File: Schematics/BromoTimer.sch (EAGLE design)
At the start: 29 parts, among them IC1 PIC16F687, IC2 7805TV, K1 G2R2A, K2 G2R2A, Q1 BC548B, Q2 BC548B, Q3 BC548B, X1 AC_IN, X4 22-23-2041, X5 AC_OUT

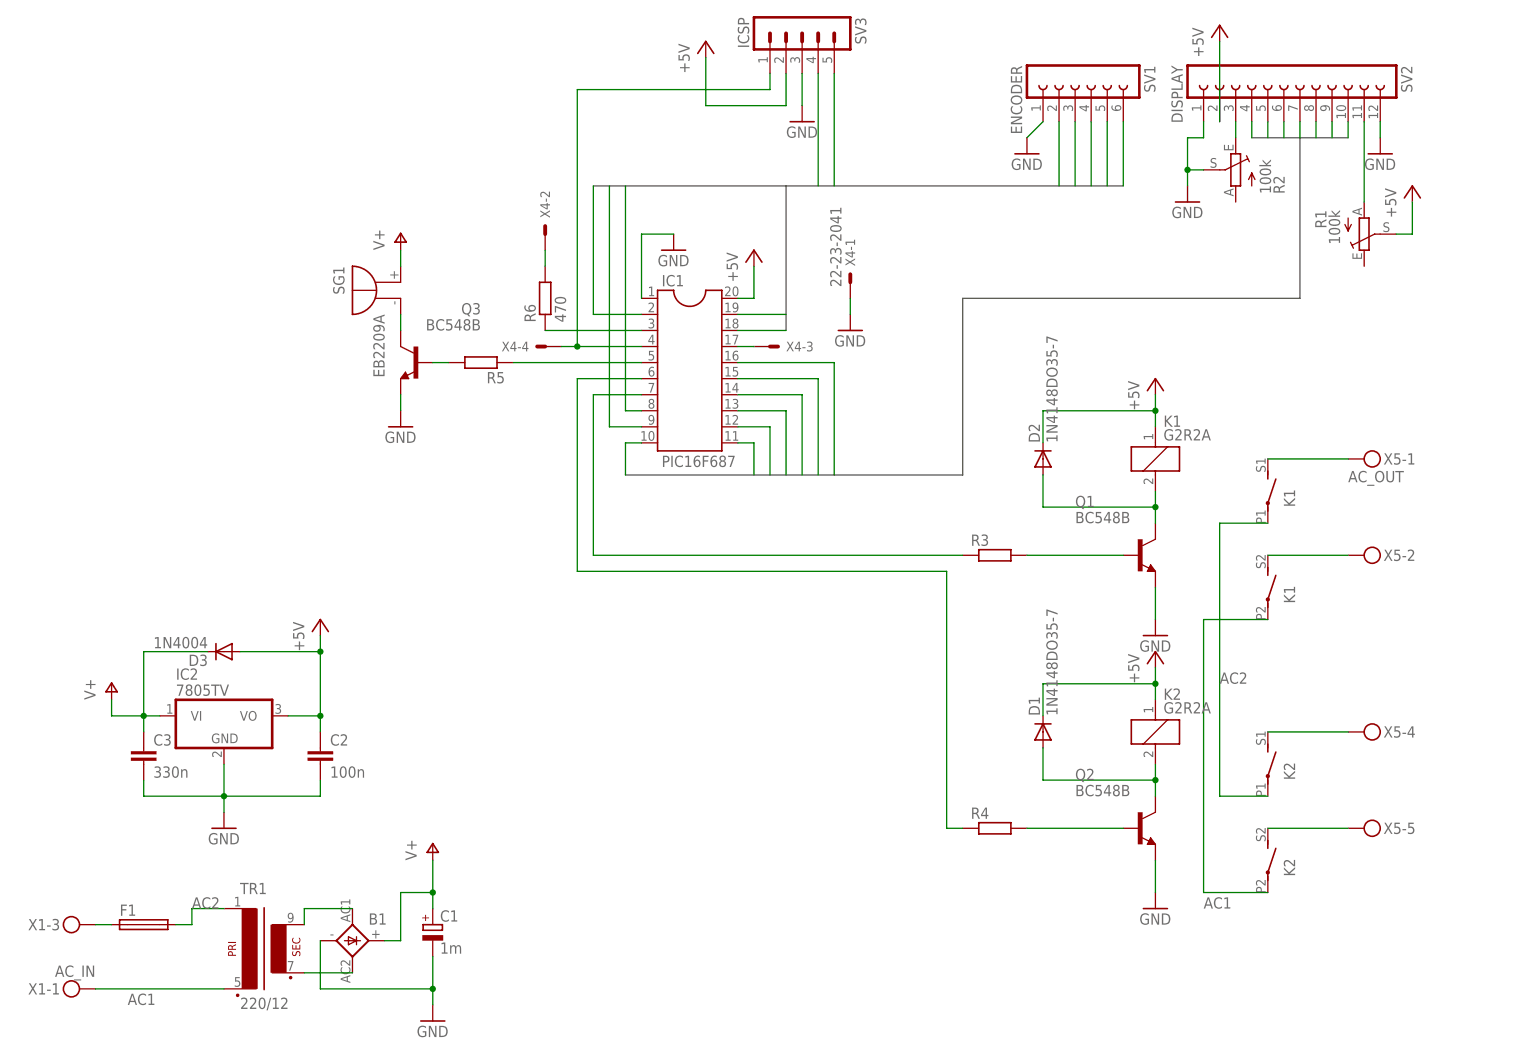
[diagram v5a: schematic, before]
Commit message: New PCB prototype
The new PCB is a little taller and a lot less wide. It has extra space for the
7805 heatsink. Connector layout should be better, too.
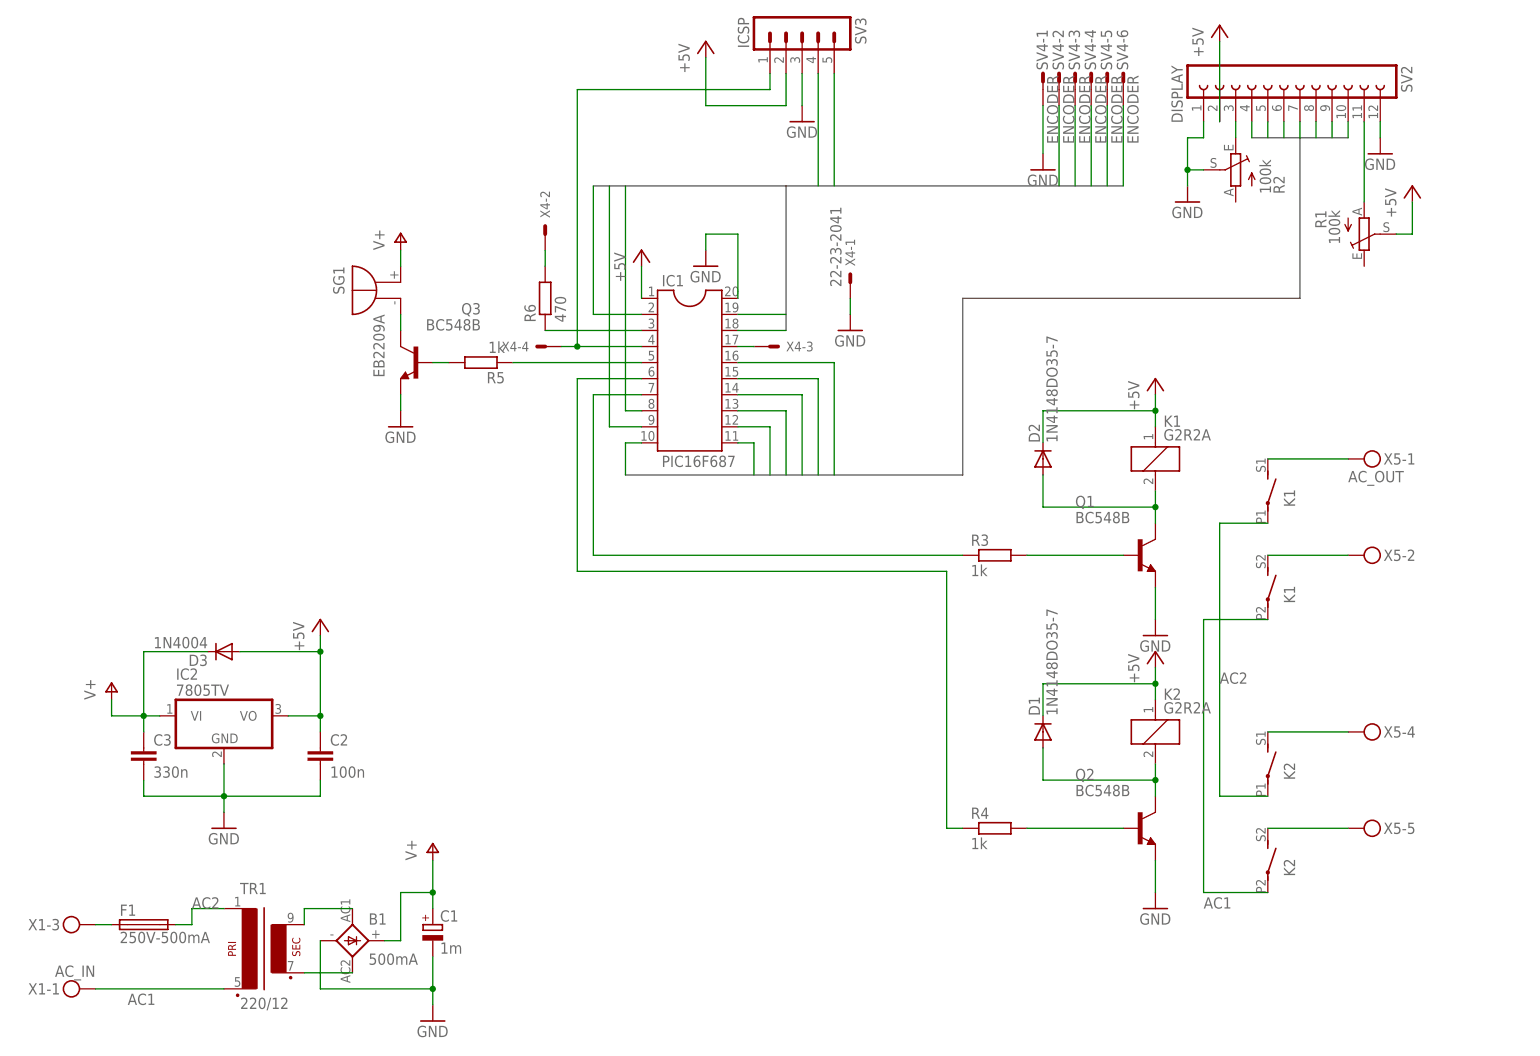
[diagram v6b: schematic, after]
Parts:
- removed SV1: ENCODER, con-lsta:FE06-1
- added SV4: ENCODER, con-amp-mt:L06P
- B1: value (none) -> 500mA
- F1: value (none) -> 250V-500mA
- R1, R2: device pot:TRIM_EU-CA14H -> pot:TRIM_EU-CA6V
- R3, R4, R5: value (none) -> 1k
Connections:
- net +5V: now also IC1.1; no longer IC1.20
- net A: now also SV4-5.S; no longer SV1.5
- net B: now also SV4-6.S; no longer SV1.6
- net GND: now also IC1.20, SV4-1.S; no longer IC1.1, SV1.1
- net L1: now also SV4-2.S; no longer SV1.2
- net L2: now also SV4-3.S; no longer SV1.3
- net SW: now also SV4-4.S; no longer SV1.4
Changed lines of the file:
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@@
 </variantdefs>
 <classes>
-<class number="0" name="default" width="0.4064" drill="0">
-<clearance class="0" value="0.635"/>
+<class number="0" name="default" width="0.3048" drill="0">
+<clearance class="0" value="0.254"/>
 </class>
 <class number="1" name="HV" width="1.27" drill="0">
-<clearance class="1" value="1.27"/>
+<clearance class="1" value="0.635"/>
 </class>
 </classes>
@@
 <part name="IC1" library="ic-package" deviceset="DIL20" device="S" value="PIC16F687"/>
 <part name="FRAME1" library="frames" deviceset="A4L-LOC" device="" value="Draft2"/>
-<part name="SV1" library="con-lsta" deviceset="FE06-1" device="" value="ENCODER"/>
 <part name="SV2" library="con-lsta" deviceset="FE12-1" device="" value="DISPLAY"/>
 <part name="IC2" library="linear" deviceset="78*" device="TV" technology="05"/>
@@
 <part name="GND4" library="supply1" deviceset="GND" device=""/>
 <part name="P+3" library="supply1" deviceset="+5V" device=""/>
-<part name="R1" library="pot" deviceset="TRIM_EU-" device="CA14H" value="100k"/>
-<part name="R2" library="pot" deviceset="TRIM_EU-" device="CA14H" value="100k"/>
+<part name="R1" library="pot" deviceset="TRIM_EU-" device="CA6V" value="100k"/>
+<part name="R2" library="pot" deviceset="TRIM_EU-" device="CA6V" value="100k"/>
 <part name="P+4" library="supply1" deviceset="+5V" device=""/>
 <part name="Q1" library="transistor-npn" deviceset="BC548*" device="" technology="B" value="BC548B"/>
 <part name="Q2" library="transistor-npn" deviceset="BC548*" device="" technology="B" value="BC548B"/>
-<part name="R3" library="rcl" deviceset="R-EU_" device="0207/10"/>
-<part name="R4" library="rcl" deviceset="R-EU_" device="0207/10"/>
+<part name="R3" library="rcl" deviceset="R-EU_" device="0207/10" value="1k"/>
+<part name="R4" library="rcl" deviceset="R-EU_" device="0207/10" value="1k"/>
 <part name="GND5" library="supply1" deviceset="GND" device=""/>
 <part name="GND6" library="supply1" deviceset="GND" device=""/>
@@
 <attribute name="OC_NEWARK" value="36M5257"/>
 </part>
-<part name="B1" library="rectifier" deviceset="2KBB-R" device=""/>
+<part name="B1" library="rectifier" deviceset="2KBB-R" device="" value="500mA"/>
 <part name="P+7" library="supply1" deviceset="V+" device=""/>
 <part name="GND7" library="supply1" deviceset="GND" device=""/>
@@
 <part name="D3" library="diode" deviceset="1N4004" device=""/>
 <part name="Q3" library="transistor-npn" deviceset="BC548*" device="" technology="B" value="BC548B"/>
-<part name="R5" library="rcl" deviceset="R-EU_" device="0207/10"/>
+<part name="R5" library="rcl" deviceset="R-EU_" device="0207/10" value="1k"/>
 <part name="GND11" library="supply1" deviceset="GND" device=""/>
 <part name="P+10" library="supply1" deviceset="V+" device=""/>
@@
 <part name="X1" library="con-phoenix-508" deviceset="MKDSN1,5/3-5,08" device="" value="AC_IN"/>
 <part name="X5" library="con-phoenix-508" deviceset="MKDSN1,5/5-5,08" device="" value="AC_OUT"/>
-<part name="F1" library="fuse" deviceset="SH22" device="">
+<part name="F1" library="fuse" deviceset="SH22" device="" value="250V-500mA">
 <attribute name="MPN" value=""/>
 <attribute name="OC_FARNELL" value="unknown"/>
 <attribute name="OC_NEWARK" value="unknown"/>
 </part>
+<part name="SV4" library="con-amp-mt" deviceset="L06P" device="" value="ENCODER"/>
 </parts>
 <sheets>
@@
 <instance part="IC1" gate="G$1" x="114.3" y="116.84"/>
 <instance part="FRAME1" gate="G$1" x="0" y="0"/>
-<instance part="SV1" gate="G$1" x="175.26" y="162.56" rot="R270"/>
 <instance part="SV2" gate="G$1" x="208.28" y="162.56" rot="R270"/>
 <instance part="IC2" gate="A1" x="40.64" y="60.96"/>
@@
 <instance part="C1" gate="G$1" x="73.66" y="27.94"/>
 <instance part="C2" gate="G$1" x="55.88" y="55.88"/>
-<instance part="GND2" gate="1" x="111.76" y="134.62"/>
-<instance part="P+2" gate="1" x="124.46" y="134.62"/>
+<instance part="GND2" gate="1" x="116.84" y="132.08"/>
+<instance part="P+2" gate="1" x="106.68" y="134.62"/>
 <instance part="GND3" gate="1" x="193.04" y="142.24"/>
 <instance part="GND4" gate="1" x="223.52" y="149.86"/>
@@
 <instance part="GND7" gate="1" x="73.66" y="12.7"/>
 <instance part="P+8" gate="1" x="22.86" y="66.04"/>
-<instance part="GND8" gate="1" x="167.64" y="149.86"/>
+<instance part="GND8" gate="1" x="170.18" y="147.32"/>
 <instance part="P+5" gate="1" x="187.96" y="71.12"/>
 <instance part="P+6" gate="1" x="187.96" y="114.3"/>
@@
 <instance part="F1" gate="1" x="27.94" y="27.94"/>
 <instance part="X4" gate="-4" x="91.44" y="119.38" rot="R180"/>
+<instance part="SV4" gate="-1" x="170.18" y="162.56" rot="MR270"/>
+<instance part="SV4" gate="-2" x="172.72" y="162.56" rot="MR270"/>
+<instance part="SV4" gate="-3" x="175.26" y="162.56" rot="MR270"/>
+<instance part="SV4" gate="-4" x="177.8" y="162.56" rot="MR270"/>
+<instance part="SV4" gate="-5" x="180.34" y="162.56" rot="MR270"/>
+<instance part="SV4" gate="-6" x="182.88" y="162.56" rot="MR270"/>
 </instances>
 <busses>
@@
 <nets>
 <net name="+5V" class="0">
-<segment>
-<pinref part="P+2" gate="1" pin="+5V"/>
-<wire x1="124.46" y1="132.08" x2="124.46" y2="127" width="0.1524" layer="91"/>
-<pinref part="IC1" gate="G$1" pin="20"/>
-<wire x1="124.46" y1="127" x2="121.92" y2="127" width="0.1524" layer="91"/>
-</segment>
 <segment>
 <pinref part="SV2" gate="G$1" pin="2"/>
@@
 <wire x1="228.6" y1="137.16" x2="226.06" y2="137.16" width="0.1524" layer="91"/>
 </segment>
+<segment>
+<pinref part="IC1" gate="G$1" pin="1"/>
+<pinref part="P+2" gate="1" pin="+5V"/>
+<wire x1="106.68" y1="127" x2="106.68" y2="132.08" width="0.1524" layer="91"/>
+</segment>
 </net>
 <net name="GND" class="0">
@@
 </segment>
 <segment>
-<pinref part="IC1" gate="G$1" pin="1"/>
-<pinref part="GND2" gate="1" pin="GND"/>
-<wire x1="106.68" y1="127" x2="106.68" y2="137.16" width="0.1524" layer="91"/>
-<wire x1="106.68" y1="137.16" x2="111.76" y2="137.16" width="0.1524" layer="91"/>
-</segment>
-<segment>
 <pinref part="SV2" gate="G$1" pin="1"/>
 <pinref part="GND3" gate="1" pin="GND"/>
@@
 </segment>
 <segment>
-<pinref part="SV1" gate="G$1" pin="1"/>
-<pinref part="GND8" gate="1" pin="GND"/>
-<wire x1="170.18" y1="154.94" x2="167.64" y2="152.4" width="0.1524" layer="91"/>
-</segment>
-<segment>
 <pinref part="SV3" gate="G$1" pin="3"/>
 <pinref part="GND10" gate="1" pin="GND"/>
@@
 <wire x1="139.7" y1="124.46" x2="139.7" y2="127" width="0.1524" layer="91"/>
 </segment>
+<segment>
+<pinref part="IC1" gate="G$1" pin="20"/>
+<wire x1="121.92" y1="127" x2="121.92" y2="137.16" width="0.1524" layer="91"/>
+<pinref part="GND2" gate="1" pin="GND"/>
+<wire x1="121.92" y1="137.16" x2="116.84" y2="137.16" width="0.1524" layer="91"/>
+<wire x1="116.84" y1="137.16" x2="116.84" y2="134.62" width="0.1524" layer="91"/>
+</segment>
+<segment>
+<pinref part="GND8" gate="1" pin="GND"/>
+<pinref part="SV4" gate="-1" pin="S"/>
+<wire x1="170.18" y1="157.48" x2="170.18" y2="149.86" width="0.1524" layer="91"/>
+</segment>
 </net>
 <net name="RS" class="0">
@@
 <net name="L1" class="0">
 <segment>
-<pinref part="SV1" gate="G$1" pin="2"/>
-<wire x1="172.72" y1="154.94" x2="172.72" y2="144.78" width="0.1524" layer="91"/>
+<wire x1="172.72" y1="157.48" x2="172.72" y2="144.78" width="0.1524" layer="91"/>
+<pinref part="SV4" gate="-2" pin="S"/>
 </segment>
 <segment>
@@
 <net name="L2" class="0">
 <segment>
-<pinref part="SV1" gate="G$1" pin="3"/>
-<wire x1="175.26" y1="154.94" x2="175.26" y2="144.78" width="0.1524" layer="91"/>
+<wire x1="175.26" y1="157.48" x2="175.26" y2="144.78" width="0.1524" layer="91"/>
+<pinref part="SV4" gate="-3" pin="S"/>
 </segment>
 <segment>
@@
 <net name="SW" class="0">
 <segment>
-<pinref part="SV1" gate="G$1" pin="4"/>
-<wire x1="177.8" y1="154.94" x2="177.8" y2="144.78" width="0.1524" layer="91"/>
+<wire x1="177.8" y1="157.48" x2="177.8" y2="144.78" width="0.1524" layer="91"/>
+<pinref part="SV4" gate="-4" pin="S"/>
 </segment>
 <segment>
@@
 <net name="A" class="0">
 <segment>
-<pinref part="SV1" gate="G$1" pin="5"/>
-<wire x1="180.34" y1="154.94" x2="180.34" y2="144.78" width="0.1524" layer="91"/>
+<wire x1="180.34" y1="157.48" x2="180.34" y2="144.78" width="0.1524" layer="91"/>
+<pinref part="SV4" gate="-5" pin="S"/>
 </segment>
 <segment>
@@
 <net name="B" class="0">
 <segment>
-<pinref part="SV1" gate="G$1" pin="6"/>
-<wire x1="182.88" y1="154.94" x2="182.88" y2="144.78" width="0.1524" layer="91"/>
+<pinref part="SV4" gate="-6" pin="S"/>
+<wire x1="182.88" y1="144.78" x2="182.88" y2="157.48" width="0.1524" layer="91"/>
 </segment>
 <segment>
@@
 </segment>
 </net>
-<net name="N$22" class="0">
+<net name="N$22" class="1">
 <segment>
 <pinref part="X1" gate="-3" pin="KL"/>

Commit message: Custom PIC part, minor layout changes
Schematic:
- changed encoder connector to right angle type
- rewired trimmer for LCD contrast, it needs to vary voltage, not resistance
- add net class for power line, specifying 24thou width and 12thou keepout
- LCD trimmers are 10k, not 100k
- add decoupling cap to IC1
- rename bus lines to LR and LG instead of L1 and L2
Board:
- moved power components on a slightly better place
- aligned diodes and resistors
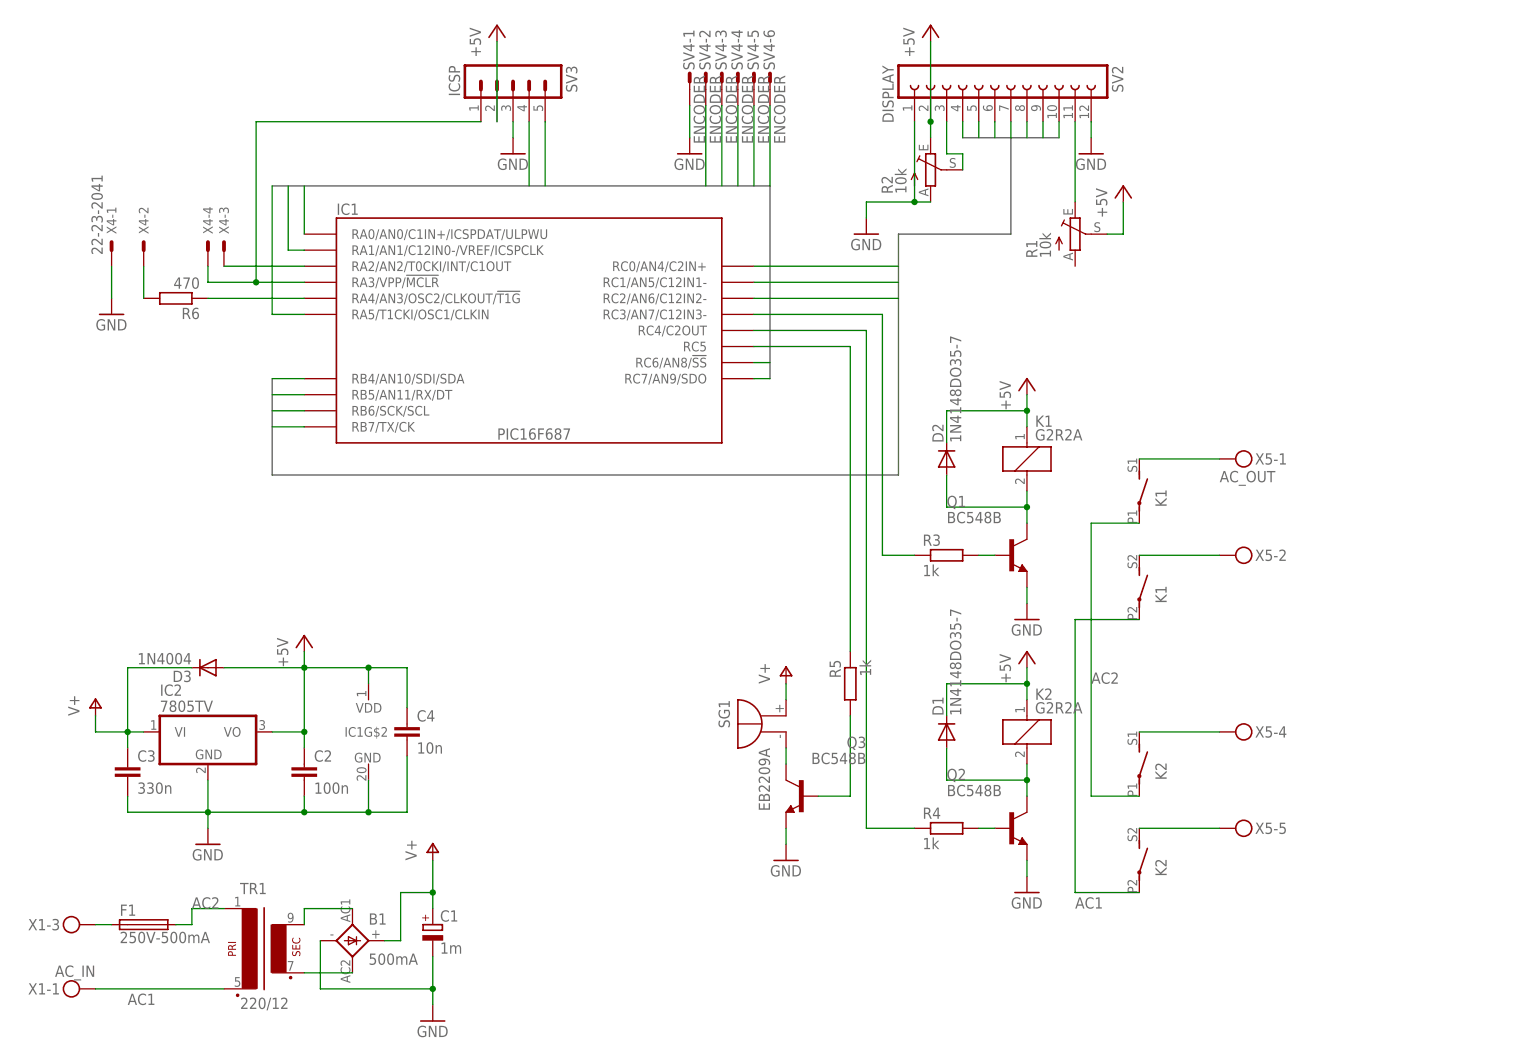
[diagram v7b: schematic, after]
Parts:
- added C4: 10n, rcl:C-EU025-024X044
- IC1: device ic-package:DIL20S -> g5pwlib:PIC16F687
- R1, R2: value 100k -> 10k
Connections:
- removed net L1: IC1.9, SV4-2.S
- removed net L2: IC1.8, SV4-3.S
- new net LG: IC1G$1.RC7/AN9/SDO, SV4-2.S
- new net LR: IC1G$1.RC6/AN8/!SS, SV4-3.S
- net +5V: now also C4.1, IC1G$2.VDD, R2.E; no longer IC1.1
- net A: now also IC1G$1.RA0/AN0/C1IN+/ICSPDAT/ULPWU; no longer IC1.19
- net B: now also IC1G$1.RA1/AN1/C12IN0-/VREF/ICSPCLK; no longer IC1.18
- net B0: now also IC1G$1.RB4/AN10/SDI/SDA; no longer IC1.13
- net B1: now also IC1G$1.RB5/AN11/RX/DT; no longer IC1.12
- net B2: now also IC1G$1.RB6/SCK/SCL; no longer IC1.11
- net B3: now also IC1G$1.RB7/TX/CK; no longer IC1.10
- net EN: now also IC1G$1.RC0/AN4/C2IN+; no longer IC1.16
- net GND: now also C4.2, IC1G$2.GND, R2.A; no longer IC1.20, R2.S
- net N$1: now also R1.E; no longer R1.A
- net N$13: now also IC1G$1.RA2/AN2/T0CKI/INT/C1OUT; no longer IC1.17
- net N$14: now also IC1G$1.RC4/C2OUT; no longer IC1.6
- net N$15: now also IC1G$1.RA3/VPP/!MCLR; no longer IC1.4
- net N$16: now also IC1G$1.RC3/AN7/C12IN3-; no longer IC1.7
- net N$17: now also IC1G$1.RC5; no longer IC1.5
- net N$20: now also IC1G$1.RA4/AN3/OSC2/CLKOUT/!T1G; no longer IC1.3
- net N$3: now also R2.S; no longer R2.E
- net RS: now also IC1G$1.RC1/AN5/C12IN1-; no longer IC1.15
- net RW: now also IC1G$1.RC2/AN6/C12IN2-; no longer IC1.14
- net SW: now also IC1G$1.RA5/T1CKI/OSC1/CLKIN; no longer IC1.2
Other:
- moved on the sheet: C2, C3, D1, D2, D3, IC2, K1, K2, Q1, Q2, Q3, R1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
